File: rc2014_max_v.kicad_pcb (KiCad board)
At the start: 2 copper layers, 101.6 x 50.8 mm, 110 parts, among them J1 Conn_01x39, J2 Conn_01x10, J3 Conn_01x06, J4 M3 Mounting Hole, J5 AVR-JTAG-10, J6 Conn_01x06, J7 USB_B_Micro, J8 Pro Bus, J9 Conn_02x04_Counter_Clockwise, SW2 SW_Push, SW3 SW_Push, SW4 SW_Push, U1 MIC5356-SGYMME, U10 SN74ALVC164245DGG, U11 IS61LV5128AL-10TLI, U2 SN74ALVC164245DGG, U3 SN74ALVC164245DGG, U4 SN74ALVC164245DGG, U5 5M570ZT100I5N, U6 TPD2EUSB30, U7 FT2232H, U8 MIC5356-SGYMME, U9 93LCxxBxxOT, X1 CB3LV-3I-50M0000, Y1 CTS-445 12Mhz

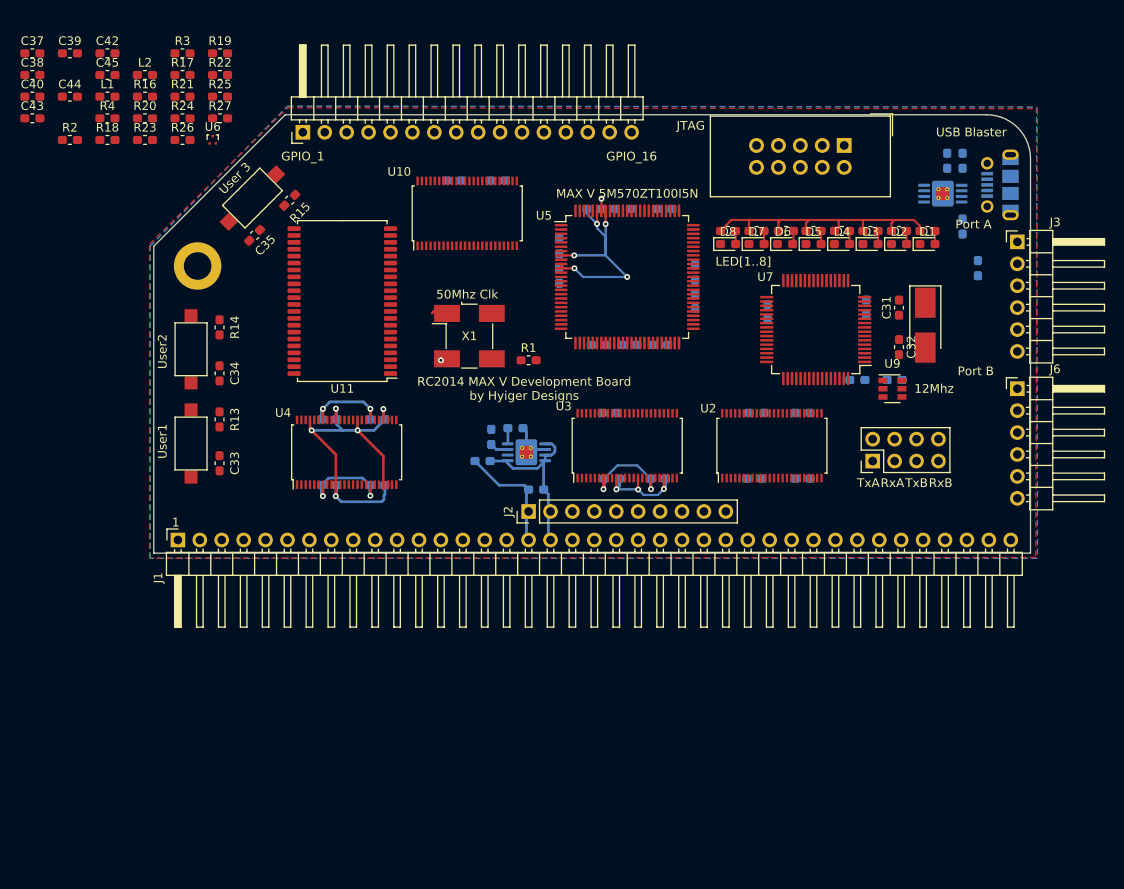
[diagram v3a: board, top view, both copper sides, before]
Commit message: replaced single resistors with arrays
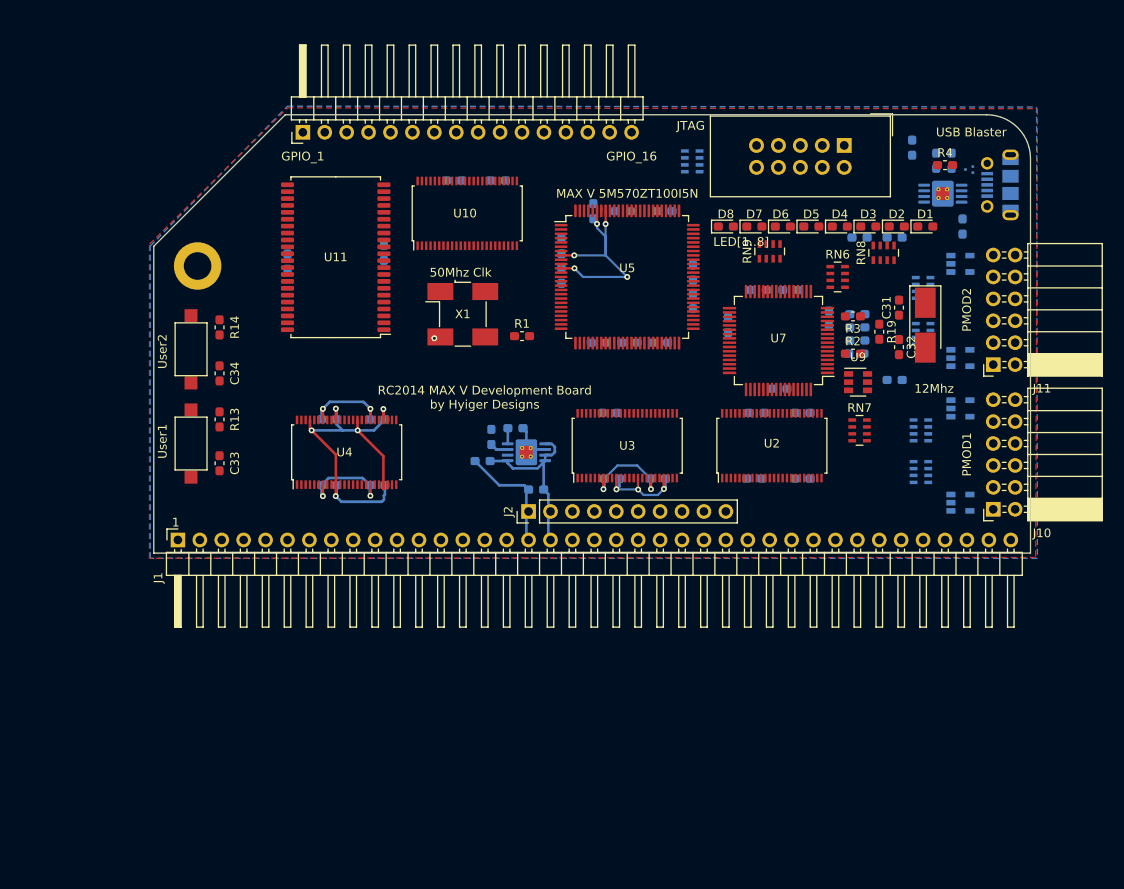
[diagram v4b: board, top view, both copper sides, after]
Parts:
- removed C35: 100nF, Capacitor_SMD:C_0603_1608Metric_Pad1.05x0.95mm_HandSolder
- removed J3, J6: Conn_01x06, Connector_PinHeader_2.54mm:PinHeader_1x06_P2.54mm_Horizontal
- removed J9: Conn_02x04_Counter_Clockwise, Connector_PinHeader_2.54mm:PinHeader_2x04_P2.54mm_Vertical
- removed R10, R11, R12, R5, R6, R7, R8, R9: 220, Resistor_SMD:R_0603_1608Metric_Pad1.05x0.95mm_HandSolder
- removed R15, R16, R17, R18, R20, R21, R22, R23: 10K, Resistor_SMD:R_0603_1608Metric_Pad1.05x0.95mm_HandSolder
- removed R24, R25, R26, R27: 22R, Resistor_SMD:R_0603_1608Metric_Pad1.05x0.95mm_HandSolder
- removed SW4: SW_Push, Button_Switch_SMD:SW_SPST_CK_RS282G05A3
- added D10: SP0504BAHT, Package_TO_SOT_SMD:SOT-23-5, B.Cu at (168.9, 110.7)
- added D12: SP0504BAHT, Package_TO_SOT_SMD:SOT-23-5, B.Cu at (168.9, 104.9)
- added D13: SP0504BAHT, Package_TO_SOT_SMD:SOT-23-5, B.Cu at (168.9, 94.0)
- added D9: SP0504BAHT, Package_TO_SOT_SMD:SOT-23-5, B.Cu at (168.9, 121.7)
- added J10: PMOD, Connector_PinSocket_2.54mm:PinSocket_2x06_P2.54mm_Horizontal, F.Cu at (172.7, 122.4)
- added J11: PMOD, Connector_PinSocket_2.54mm:PinSocket_2x06_P2.54mm_Horizontal, F.Cu at (172.7, 105.7)
- added RN1: 200R, Resistor_SMD:R_Array_Concave_4x0603, B.Cu at (164.3, 118.1)
- added RN2: 200R, Resistor_SMD:R_Array_Concave_4x0603, B.Cu at (164.3, 113.3)
- added RN3: 200R, Resistor_SMD:R_Array_Concave_4x0603, B.Cu at (164.6, 102.1)
- added RN4: 200R, Resistor_SMD:R_Array_Concave_4x0603, B.Cu at (164.6, 96.8)
- added RN5: 10K, Resistor_SMD:R_Array_Concave_4x0603, B.Cu at (137.8, 82.1)
- added RN6: 22R, Resistor_SMD:R_Array_Concave_4x0603, F.Cu at (154.7, 95.5)
- added RN7: 10K, Resistor_SMD:R_Array_Concave_4x0603, F.Cu at (157.2, 113.3)
- added RN8: 200R, Resistor_SMD:R_Array_Concave_4x0603, F.Cu at (160.0, 92.7)
- added RN9: 200R, Resistor_SMD:R_Array_Concave_4x0603, F.Cu at (146.8, 92.5)
- C37, C38, C39, C40, C42, C43, C44, C45, L1, L2, U6: moved to B.Cu
- moved C37 100.7 mm to (157.0, 101.3)
- moved C38 100.4 mm to (157.0, 102.9)
- moved C40 98.9 mm to (157.0, 99.8)
- moved C39 97.6 mm to (156.9, 104.4)
- moved R4 97.2 mm to (167.1, 82.5)
- moved R2 94.1 mm to (156.5, 104.4)
- moved L2 88.9 mm to (161.3, 90.9)
- moved L1 88.7 mm to (157.2, 90.9)
- moved U6 87.7 mm to (169.9, 83.1), turned to 270 degrees
- moved C43 86.5 mm to (145.5, 97.0)
- moved C44 86.5 mm to (149.2, 97.0), turned to 180 degrees
- moved R3 83.5 mm to (156.5, 100.1), turned to 180 degrees
- moved R19 82.9 mm to (159.5, 101.9), turned to 270 degrees
- moved C45 38.1 mm to (102.1, 92.7), turned to 90 degrees
- moved C42 31.9 mm to (90.9, 93.7), turned to 270 degrees
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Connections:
- J1 pad 35: (no net) -> TX_A
- J1 pad 36: (no net) -> RX_A
- R1 pad 2: (no net) -> IO1_CLK0
- U2 pad 37: (no net) -> ~BUSACK_F
- U2 pad 38: (no net) -> ~PAGE_F
- U2 pad 40: (no net) -> ~IORQ_F
- U2 pad 41: (no net) -> ~RD_F
- U2 pad 43: (no net) -> ~WR_F
- U2 pad 44: (no net) -> ~MREQ_F
- U2 pad 46: (no net) -> CLK_F
- U2 pad 47: (no net) -> ~M1_F
- U3 pad 12: (no net) -> RX_A
- U3 pad 24: (no net) -> TX_A
- U5 pad 12: (no net) -> IO1_CLK0
- U5 pad 14: (no net) -> CLK_F
- U5 pad 15: (no net) -> A4_F
- U5 pad 16: (no net) -> A5_F
- U5 pad 17: (no net) -> A6_F
- U5 pad 18: (no net) -> A7_F
- U5 pad 19: (no net) -> A8_F
- U5 pad 2: (no net) -> A10_F
- U5 pad 20: (no net) -> A9_F
- U5 pad 21: (no net) -> A0_F
- U5 pad 26: (no net) -> A1_F
- U5 pad 27: (no net) -> A2_F
- U5 pad 28: (no net) -> A3_F
- U5 pad 29: (no net) -> D0_F
- U5 pad 3: (no net) -> A11_F
- U5 pad 30: (no net) -> D1_F
- U5 pad 33: (no net) -> D2_F
- U5 pad 34: (no net) -> D3_F
- U5 pad 35: (no net) -> D4_F
- U5 pad 36: (no net) -> D5_F
- U5 pad 38: (no net) -> D6_F
- U5 pad 4: (no net) -> A12_F
- U5 pad 40: (no net) -> D7_F
- U5 pad 41: (no net) -> ~M1_F
- U5 pad 42: (no net) -> ~MREQ_F
- U5 pad 43: (no net) -> ~WR_F
- U5 pad 44: (no net) -> ~RD_F
- U5 pad 47: (no net) -> ~IORQ_F
- U5 pad 48: (no net) -> ~PAGE_F
- U5 pad 49: (no net) -> ~BUSACK_F
- U5 pad 5: (no net) -> A13_F
- U5 pad 52: (no net) -> ~RESET
- U5 pad 53: (no net) -> ~INT
- U5 pad 54: (no net) -> ~RESET2
- U5 pad 55: (no net) -> ~HALT
- U5 pad 56: (no net) -> ~BUSRQ
- U5 pad 57: (no net) -> ~WAIT
- U5 pad 58: (no net) -> ~NMI
- U5 pad 6: (no net) -> A14_F
- U5 pad 61: (no net) -> RX_A
- U5 pad 66: (no net) -> GPIO_1
- U5 pad 67: (no net) -> GPIO_2
- U5 pad 68: (no net) -> GPIO_3
- U5 pad 69: (no net) -> GPIO_4
- U5 pad 7: (no net) -> A15_F
- U5 pad 70: (no net) -> GPIO_5
- U5 pad 71: (no net) -> GPIO_6
- U5 pad 72: (no net) -> GPIO_7
- U5 pad 73: (no net) -> GPIO_8
- U5 pad 74: (no net) -> GPIO_9
- U5 pad 75: (no net) -> GPIO_10
- U5 pad 76: (no net) -> GPIO_11
- U5 pad 77: (no net) -> GPIO_12
- U5 pad 78: (no net) -> GPIO_13
- U5 pad 81: (no net) -> GPIO_14
- U5 pad 82: (no net) -> GPIO_15
- U5 pad 83: (no net) -> GPIO_16
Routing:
- net +3V3: track 48.1 -> 13.5 mm, vias 3 -> 2
- net GND: track 107.7 -> 106.0 mm
- net Net-(D8-Pad2): track 1.52 -> 0.00 mm
- net Net-(D7-Pad2): track 1.52 -> 0.00 mm
- net Net-(D5-Pad2): track 1.52 -> 0.00 mm
- net Net-(D4-Pad2): track 1.52 -> 0.00 mm
- net Net-(D3-Pad2): track 1.52 -> 0.00 mm
- net Net-(D2-Pad2): track 1.52 -> 0.00 mm
- net Net-(D1-Pad2): track 1.52 -> 0.00 mm
- net Net-(D6-Pad2): track 1.57 -> 0.16 mm
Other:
- board text added: "PMOD1"
- board text added: "PMOD2"
- board text removed: "Port A"
- board text removed: "Port B"
- board text removed: "RxA"
- board text removed: "RxB"
- board text removed: "TxA"
- board text removed: "TxB"
- board text removed: "User 3"

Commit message: fixed up GPIO, started layout
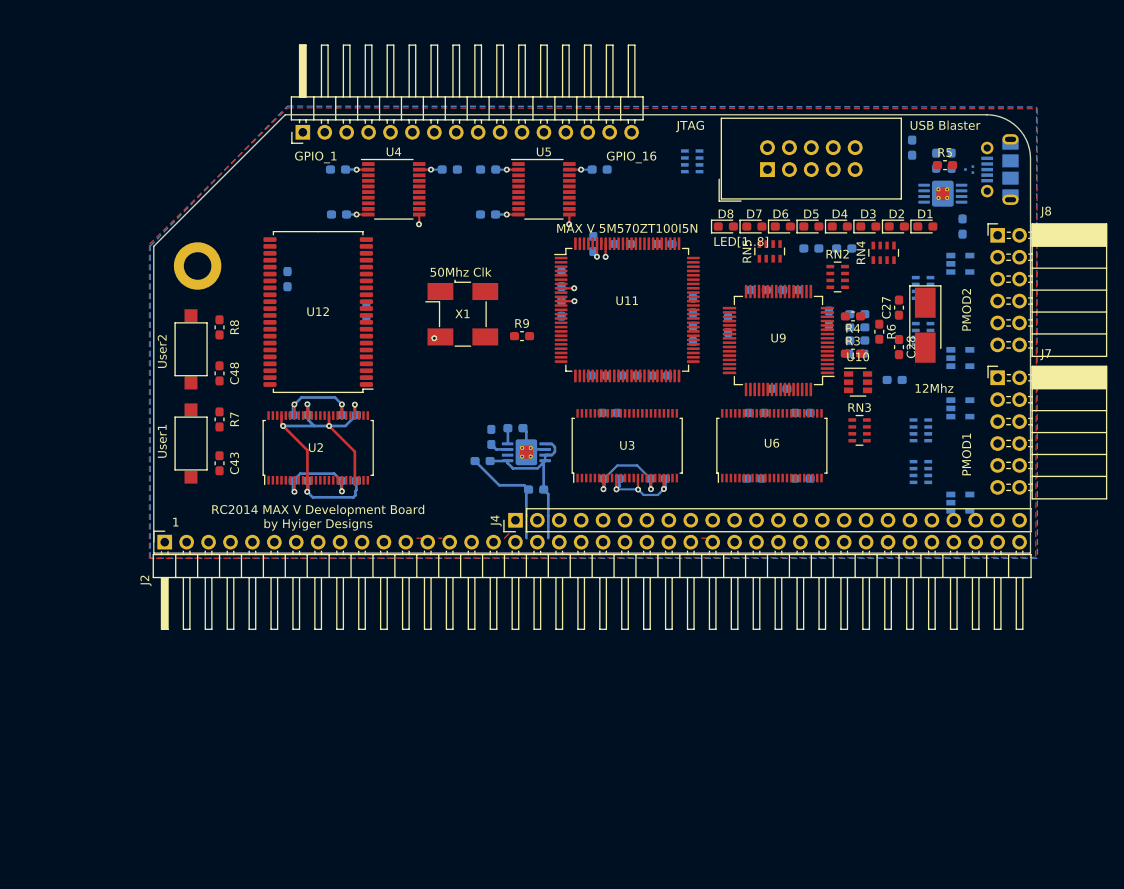
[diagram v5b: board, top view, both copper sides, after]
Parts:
- removed the C18 at (134.6, 87.9)
- removed the C19 at (137.9, 98.3)
- removed the C20 at (134.1, 103.1)
- removed the C21 at (127.0, 103.1)
- removed the C23 at (129.8, 87.9)
- removed the C24 at (137.9, 95.0)
- removed the C25 at (130.6, 103.1)
- removed the J1 at (78.2, 126.0)
- removed J10, J11: PMOD, Connector_PinSocket_2.54mm:PinSocket_2x06_P2.54mm_Horizontal
- removed the U10 at (111.8, 88.1)
- added C16: 100nF, Capacitor_SMD:C_0603_1608Metric_Pad1.05x0.95mm_HandSolder, B.Cu at (109.7, 83.1)
- added C36: 100nF, Capacitor_SMD:C_0603_1608Metric_Pad1.05x0.95mm_HandSolder, B.Cu at (126.4, 91.7)
- added C37: 100nF, Capacitor_SMD:C_0603_1608Metric_Pad1.05x0.95mm_HandSolder, B.Cu at (134.6, 91.7)
- added C38: 100nF, Capacitor_SMD:C_0603_1608Metric_Pad1.05x0.95mm_HandSolder, B.Cu at (137.9, 102.1)
- added C39: 100nF, Capacitor_SMD:C_0603_1608Metric_Pad1.05x0.95mm_HandSolder, B.Cu at (134.1, 106.9)
- added C40: 100nF, Capacitor_SMD:C_0603_1608Metric_Pad1.05x0.95mm_HandSolder, B.Cu at (127.0, 106.9)
- added C44: 100nF, Capacitor_SMD:C_0603_1608Metric_Pad1.05x0.95mm_HandSolder, B.Cu at (129.8, 91.7)
- added C45: 100nF, Capacitor_SMD:C_0603_1608Metric_Pad1.05x0.95mm_HandSolder, B.Cu at (137.9, 98.8)
- added C46: 100nF, Capacitor_SMD:C_0603_1608Metric_Pad1.05x0.95mm_HandSolder, B.Cu at (130.6, 106.9)
- added J4: Conn_01x24, Connector_PinHeader_2.54mm:PinHeader_1x24_P2.54mm_Vertical, F.Cu at (117.3, 123.7)
- added J7: PMOD, Connector_PinSocket_2.54mm:PinSocket_2x06_P2.54mm_Horizontal, F.Cu at (173.2, 107.2)
- added J8: PMOD, Connector_PinSocket_2.54mm:PinSocket_2x06_P2.54mm_Horizontal, F.Cu at (173.2, 90.7)
- added R1: 50K, Resistor_SMD:R_0603_1608Metric_Pad1.05x0.95mm_HandSolder, B.Cu at (96.9, 88.3)
- added R2: 50K, Resistor_SMD:R_0603_1608Metric_Pad1.05x0.95mm_HandSolder, B.Cu at (114.2, 88.3)
- added U4: TXB0108PWR, Package_SO:TSSOP-20_4.4x6.5mm_P0.65mm, F.Cu at (103.3, 85.3)
- added U5: TXB0108PWR, Package_SO:TSSOP-20_4.4x6.5mm_P0.65mm, F.Cu at (120.7, 85.3)
- J2: value Conn_01x10 -> Conn_01x40; footprint Connector_PinHeader_2.54mm:PinHeader_1x10_P2.54mm_Vertical -> Connector_PinHeader_2.54mm:PinHeader_1x40_P2.54mm_Horizontal
- moved C42 13.5 mm to (96.8, 83.1), turned to 180 degrees
- moved L2 9.74 mm to (151.6, 92.2)
- moved J5 9.32 mm to (146.6, 83.1), turned to 90 degrees
- moved C32 7.15 mm to (100.1, 99.6)
- moved U12 6.67 mm to (94.5, 99.6)
- moved J2 6.51 mm to (125.0, 125.0), turned to 0 degrees
- moved C17 4.88 mm to (127.1, 83.1), turned to 0 degrees
- moved C41 3.81 mm to (122.7, 95.8)
- moved C47 3.81 mm to (122.7, 99.2)
- moved U11 3.81 mm to (130.3, 99.3)
- moved C11 3.34 mm to (98.0, 119.1)
- moved C2 3.34 mm to (98.0, 111.5)
- moved U2 3.34 mm to (94.5, 115.3)
- moved C1 3.34 mm to (92.5, 111.5)
- moved C10 3.34 mm to (92.5, 119.1)
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- renumbered C11 to C1, C5 to C10, C6 to C11, C7 to C12, C8 to C13, C9 to C14, C10 to C15, C1 to C18, C37 to C19, C12 to C2, C38 to C20, C39 to C21, C40 to C22, C28 to C23, C29 to C24, C30 to C25, C41 to C26, C31 to C27, C32 to C28, C42 to C29, C13 to C3, C43 to C30, C44 to C31, C45 to C32, C46 to C33, C47 to C34, C48 to C35, C14 to C4, C22 to C41, C36 to C42, C33 to C43, C26 to C47, C34 to C48, C27 to C49, C15 to C5, C16 to C6, C3 to C7, C2 to C8, C4 to C9, D13 to D10, D9 to D11, D10 to D12, D12 to D9, J4 to J1, J8 to J3, J7 to J6, R2 to R3, R3 to R4, R4 to R5, R19 to R6, R13 to R7, R14 to R8, R1 to R9, RN5 to RN1, RN6 to RN2, RN7 to RN3, RN8 to RN4, RN9 to RN5, RN3 to RN6, RN4 to RN7, RN1 to RN8, RN2 to RN9, SW2 to SW1, SW3 to SW2, U9 to U10, U5 to U11, U11 to U12, U4 to U2, U2 to U6, U8 to U7, U6 to U8, U7 to U9
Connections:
- C17 pad 1: +3V3 -> 5V
- D1 pad 1: (no net) -> LED1
- D2 pad 1: (no net) -> LED2
- D3 pad 1: (no net) -> LED3
- D4 pad 1: (no net) -> LED4
- D5 pad 1: (no net) -> LED5
- D6 pad 1: (no net) -> LED6
- D7 pad 1: (no net) -> LED7
- D8 pad 1: (no net) -> LED8
- J2 pad 1: GND -> A15
- J2 pad 10: ~NMI -> A6
- J2 pad 2: 5V -> A14
- J2 pad 3: ~PAGE -> A13
- J2 pad 4: ~RESET2 -> A12
- J2 pad 5: (no net) -> A11
- J2 pad 6: ~BUSACK -> A10
- J2 pad 7: ~HALT -> A9
- J2 pad 8: ~BUSRQ -> A8
- J2 pad 9: ~WAIT -> A7
- J5 pad 4: (no net) -> Net-(J5-Pad4)
- J5 pad 6: (no net) -> Net-(J5-Pad6)
- J5 pad 7: (no net) -> Net-(J5-Pad7)
- J5 pad 8: (no net) -> Net-(J5-Pad8)
- RN3 pad 4: (no net) -> Net-(RN3-Pad4)
- RN6 pad 5: (no net) -> GPIO_4
- RN6 pad 6: (no net) -> GPIO_3
- RN6 pad 7: (no net) -> GPIO_2
- RN6 pad 8: (no net) -> GPIO_1
- RN7 pad 5: (no net) -> GPIO_8
- RN7 pad 6: (no net) -> GPIO_7
- RN7 pad 7: (no net) -> GPIO_6
- RN7 pad 8: (no net) -> GPIO_5
- RN8 pad 5: (no net) -> GPIO_13
- RN8 pad 6: (no net) -> GPIO_12
- RN8 pad 7: (no net) -> GPIO_11
- RN8 pad 8: (no net) -> GPIO_10
- RN9 pad 5: (no net) -> GPIO_16
- RN9 pad 6: (no net) -> GPIO_15
- RN9 pad 7: (no net) -> GPIO_14
- RN9 pad 8: (no net) -> GPIO_13
- U1 pad 6: (no net) -> Net-(U1-Pad6)
- U11 pad 1: (no net) -> GPIO_16
- U11 pad 100: (no net) -> GPIO_15
- U11 pad 22: (no net) -> Net-(U11-Pad22)
- U11 pad 23: (no net) -> Net-(U11-Pad23)
- U11 pad 24: (no net) -> Net-(U11-Pad24)
- U11 pad 25: (no net) -> Net-(U11-Pad25)
- U11 pad 50: (no net) -> Net-(U11-Pad50)
- U11 pad 51: (no net) -> Net-(U11-Pad51)
- U11 pad 52: ~RESET -> ~RESET_F
- U11 pad 53: ~INT -> ~INT_F
- U11 pad 54: ~RESET2 -> ~RESET2_F
- U11 pad 55: ~HALT -> ~HALT_F
- U11 pad 56: ~BUSRQ -> ~BUSRQ_F
- U11 pad 57: ~WAIT -> ~WAIT_F
- U11 pad 58: ~NMI -> ~NMI_F
- U11 pad 61: RX_A -> Net-(U11-Pad61)
- U11 pad 62: (no net) -> Net-(U11-Pad62)
- U11 pad 64: (no net) -> Net-(U11-Pad64)
- U11 pad 66: GPIO_1 -> Net-(U11-Pad66)
- U11 pad 67: GPIO_2 -> RX_A_F
- U11 pad 68: GPIO_3 -> Net-(U11-Pad68)
- U11 pad 69: GPIO_4 -> Net-(U11-Pad69)
- U11 pad 70: GPIO_5 -> Net-(U11-Pad70)
- U11 pad 71: GPIO_6 -> Net-(U11-Pad71)
- U11 pad 72: GPIO_7 -> Net-(U11-Pad72)
- U11 pad 73: GPIO_8 -> Net-(U11-Pad73)
- U11 pad 74: GPIO_9 -> Net-(U11-Pad74)
- U11 pad 75: GPIO_10 -> Net-(U11-Pad75)
- U11 pad 76: GPIO_11 -> Net-(U11-Pad76)
- U11 pad 77: GPIO_12 -> Net-(U11-Pad77)
- U11 pad 78: GPIO_13 -> Net-(U11-Pad78)
- U11 pad 81: GPIO_14 -> GPIO_1
- U11 pad 82: GPIO_15 -> GPIO_2
- U11 pad 83: GPIO_16 -> GPIO_3
- U11 pad 84: (no net) -> GPIO_4
- U11 pad 85: (no net) -> GPIO_5
- U11 pad 86: (no net) -> GPIO_6
- U11 pad 87: (no net) -> GPIO_7
- U11 pad 89: (no net) -> GPIO_8
- U11 pad 91: (no net) -> GPIO_9
- U11 pad 92: (no net) -> GPIO_10
- U11 pad 96: (no net) -> GPIO_11
- U11 pad 97: (no net) -> GPIO_12
- U11 pad 98: (no net) -> GPIO_13
- U11 pad 99: (no net) -> GPIO_14
- U12 pad 1: (no net) -> Net-(U12-Pad1)
- U12 pad 15: (no net) -> Net-(U12-Pad15)
- U12 pad 2: (no net) -> Net-(U12-Pad2)
- U12 pad 21: (no net) -> Net-(U12-Pad21)
- U12 pad 22: (no net) -> Net-(U12-Pad22)
- U12 pad 23: (no net) -> Net-(U12-Pad23)
- U12 pad 24: (no net) -> Net-(U12-Pad24)
- U12 pad 25: (no net) -> Net-(U12-Pad25)
- U12 pad 37: (no net) -> Net-(U12-Pad37)
- U12 pad 39: (no net) -> Net-(U12-Pad39)
- U12 pad 40: (no net) -> Net-(U12-Pad40)
- U12 pad 41: (no net) -> Net-(U12-Pad41)
- U12 pad 42: (no net) -> Net-(U12-Pad42)
- U12 pad 43: (no net) -> Net-(U12-Pad43)
- U12 pad 44: (no net) -> Net-(U12-Pad44)
- U12 pad 8: (no net) -> Net-(U12-Pad8)
- U3 pad 13: (no net) -> ~M1
- U3 pad 14: (no net) -> CLK
- U3 pad 16: (no net) -> ~MREQ
- U3 pad 17: (no net) -> ~WR
- U3 pad 19: (no net) -> ~RD
- U3 pad 20: (no net) -> ~IORQ
- U3 pad 22: (no net) -> ~PAGE
- U3 pad 23: (no net) -> ~BUSACK
- U3 pad 24: TX_A -> DIR
- U3 pad 25: (no net) -> OE_C_I
- U3 pad 26: (no net) -> ~BUSACK_F
- U3 pad 27: (no net) -> ~PAGE_F
- U3 pad 29: (no net) -> ~IORQ_F
- U3 pad 30: (no net) -> ~RD_F
- U3 pad 32: (no net) -> ~WR_F
- U3 pad 33: (no net) -> ~MREQ_F
- U3 pad 35: (no net) -> CLK_F
- U3 pad 36: (no net) -> ~M1_F
- U3 pad 37: (no net) -> RX_A_F
- U3 pad 38: (no net) -> ~NMI_F
- U3 pad 40: (no net) -> ~WAIT_F
- U3 pad 41: (no net) -> ~BUSRQ_F
- U3 pad 43: (no net) -> ~HALT_F
- U3 pad 44: (no net) -> ~RESET2_F
- U3 pad 46: (no net) -> ~INT_F
- U3 pad 47: (no net) -> ~RESET_F
- U3 pad 48: (no net) -> OE_C_O
- U6 pad 1: DIR -> ~DIR
- U6 pad 11: ~PAGE -> D3
- U6 pad 12: ~BUSACK -> D11
- U6 pad 13: D0 -> D4
- U6 pad 14: D1 -> D12
- U6 pad 16: D2 -> D5
- U6 pad 17: D3 -> D13
- U6 pad 19: D4 -> D6
- U6 pad 2: ~M1 -> D0
- U6 pad 20: D5 -> D14
- U6 pad 22: D6 -> D7
- U6 pad 23: D7 -> D15
- U6 pad 25: (no net) -> OE_D
- U6 pad 26: D7_F -> D15_F
- U6 pad 27: D6_F -> D7_F
- U6 pad 29: D5_F -> D14_F
- U6 pad 3: CLK -> D8
- U6 pad 30: D4_F -> D6_F
- U6 pad 32: D3_F -> D13_F
- U6 pad 33: D2_F -> D5_F
- U6 pad 35: D1_F -> D12_F
- U6 pad 36: D0_F -> D4_F
- U6 pad 37: ~BUSACK_F -> D11_F
- U6 pad 38: ~PAGE_F -> D3_F
- U6 pad 40: ~IORQ_F -> D10_F
- U6 pad 41: ~RD_F -> D2_F
- U6 pad 43: ~WR_F -> D9_F
- U6 pad 44: ~MREQ_F -> D1_F
- U6 pad 46: CLK_F -> D8_F
- U6 pad 47: ~M1_F -> D0_F
- U6 pad 48: (no net) -> OE_D
- U6 pad 5: ~MREQ -> D1
- U6 pad 6: ~WR -> D9
- U6 pad 8: ~RD -> D2
- U6 pad 9: ~IORQ -> D10
- U7 pad 6: (no net) -> Net-(U7-Pad6)
- U9 pad 21: (no net) -> Net-(U9-Pad21)
- U9 pad 22: (no net) -> Net-(U9-Pad22)
- U9 pad 23: (no net) -> Net-(U9-Pad23)
- U9 pad 24: (no net) -> Net-(U9-Pad24)
- U9 pad 26: (no net) -> Net-(U9-Pad26)
- U9 pad 27: (no net) -> Net-(U9-Pad27)
- U9 pad 28: (no net) -> Net-(U9-Pad28)
- U9 pad 29: (no net) -> Net-(U9-Pad29)
- U9 pad 30: (no net) -> Net-(U9-Pad30)
- U9 pad 32: (no net) -> Net-(U9-Pad32)
- U9 pad 33: (no net) -> Net-(U9-Pad33)
- U9 pad 34: (no net) -> Net-(U9-Pad34)
- U9 pad 36: (no net) -> Net-(U9-Pad36)
- U9 pad 38: (no net) -> Net-(U9-Pad38)
- U9 pad 39: (no net) -> Net-(U9-Pad39)
- U9 pad 40: (no net) -> Net-(U9-Pad40)
- U9 pad 41: (no net) -> Net-(U9-Pad41)
- U9 pad 43: (no net) -> Net-(U9-Pad43)
- U9 pad 44: (no net) -> Net-(U9-Pad44)
- U9 pad 45: (no net) -> Net-(U9-Pad45)
- U9 pad 46: (no net) -> Net-(U9-Pad46)
- U9 pad 48: (no net) -> Net-(U9-Pad48)
- U9 pad 49: (no net) -> Net-(U9-Pad49)
- U9 pad 50: (no net) -> Net-(U9-Pad50)
- U9 pad 52: (no net) -> Net-(U9-Pad52)
- U9 pad 53: (no net) -> Net-(U9-Pad53)
- U9 pad 54: (no net) -> Net-(U9-Pad54)
- U9 pad 55: (no net) -> Net-(U9-Pad55)
- U9 pad 57: (no net) -> Net-(U9-Pad57)
- U9 pad 58: (no net) -> Net-(U9-Pad58)
- U9 pad 59: (no net) -> Net-(U9-Pad59)
- U9 pad 60: (no net) -> Net-(U9-Pad60)
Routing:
- net GND: track 106.0 -> 87.0 mm, vias 14 -> 15
- net +3V3: track 13.5 -> 19.2 mm, vias 2 -> 4
- net 5V: track 43.9 -> 49.2 mm, vias 4 -> 6
- net OE_G_2: track 0.00 -> 2.65 mm, vias 0 -> 1
- net OE_G_1: track 0.00 -> 2.53 mm, vias 0 -> 1
- net A4: track 0.73 -> 0.00 mm
- net A3: track 0.36 -> 1.09 mm
- net ~RD: track 0.71 -> 0.00 mm
- net ~IORQ: track 0.00 -> 0.71 mm
